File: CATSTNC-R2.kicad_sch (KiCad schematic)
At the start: 64 parts, among them J1 BNC, J1 USB_C_Receptacle_USB2.0, J4 GPIO-1, J5 DC IN, J5 GPIO-2, SW1 BOOT, SW1 RESET, U1 RP2040, U1 TPS62933, U4 NCP1117-3.3_SOT223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

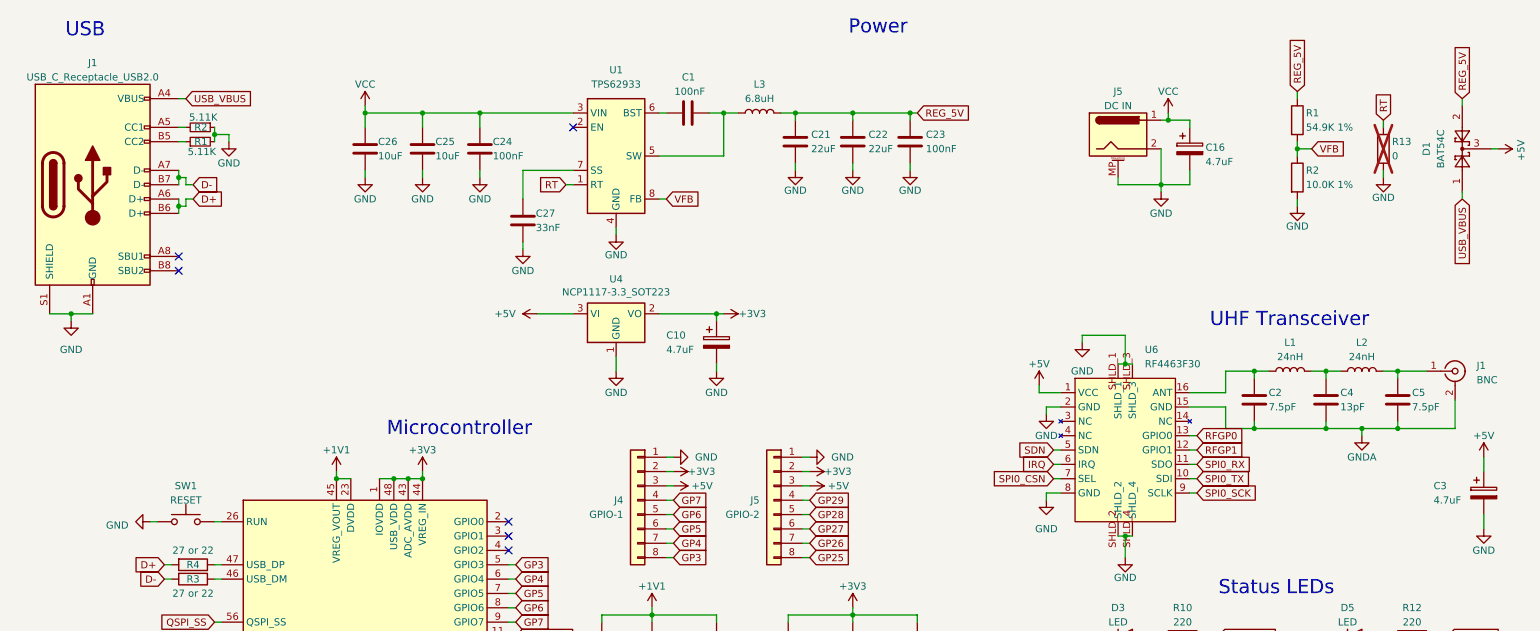
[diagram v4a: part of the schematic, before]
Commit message: Remove BAT54C
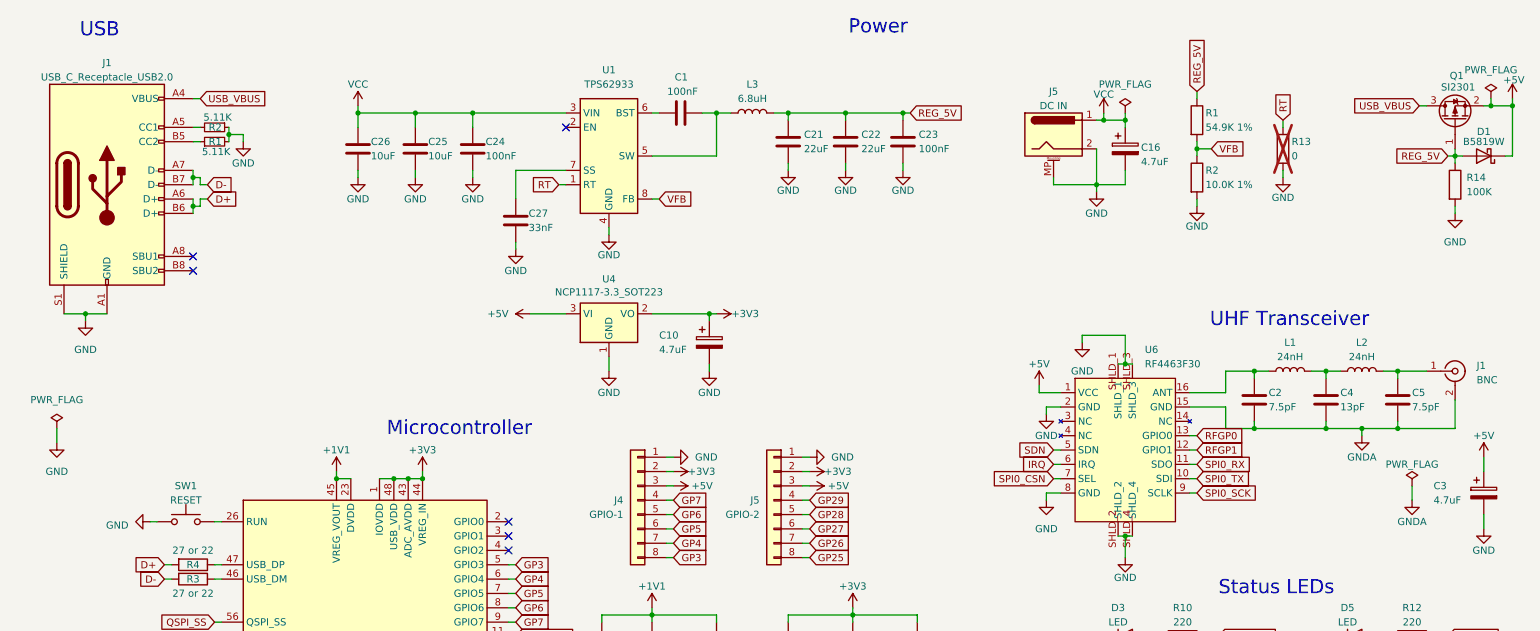
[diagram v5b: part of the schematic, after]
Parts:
- removed D1: BAT54C, Package_TO_SOT_SMD:SOT-23, symbol Diode:BAT54C
- added D1: B5819W, Diode_SMD:D_SOD-123, symbol Device:D_Schottky
- added Q1: SI2301, Package_TO_SOT_SMD:SOT-23, symbol Transistor_FET:FDN340P
- added R14: 100K, Resistor_SMD:R_0603_1608Metric, symbol Device:R
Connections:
- net +5V: now also D1.1 (K), Q1.2 (S)
- net GND: now also R14.2
- net REG_5V: now also D1.2 (A), Q1.1 (G), R14.1
- net USB_VBUS: now also Q1.3 (D)
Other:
- moved on the sheet: C1, C10, C16, C21, C22, C23, C24, C25, C26, C27, J1, J5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

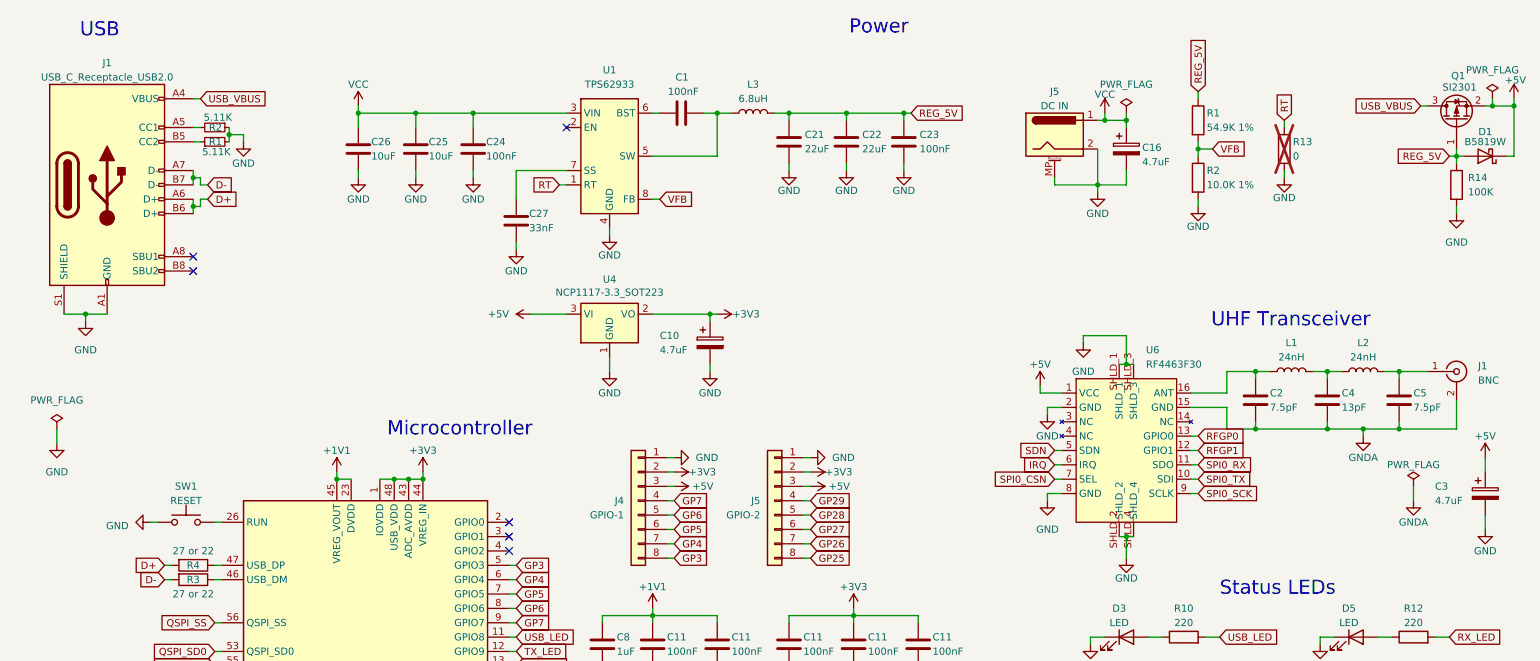
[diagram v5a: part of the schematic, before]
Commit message: Add power mux, USB TVS
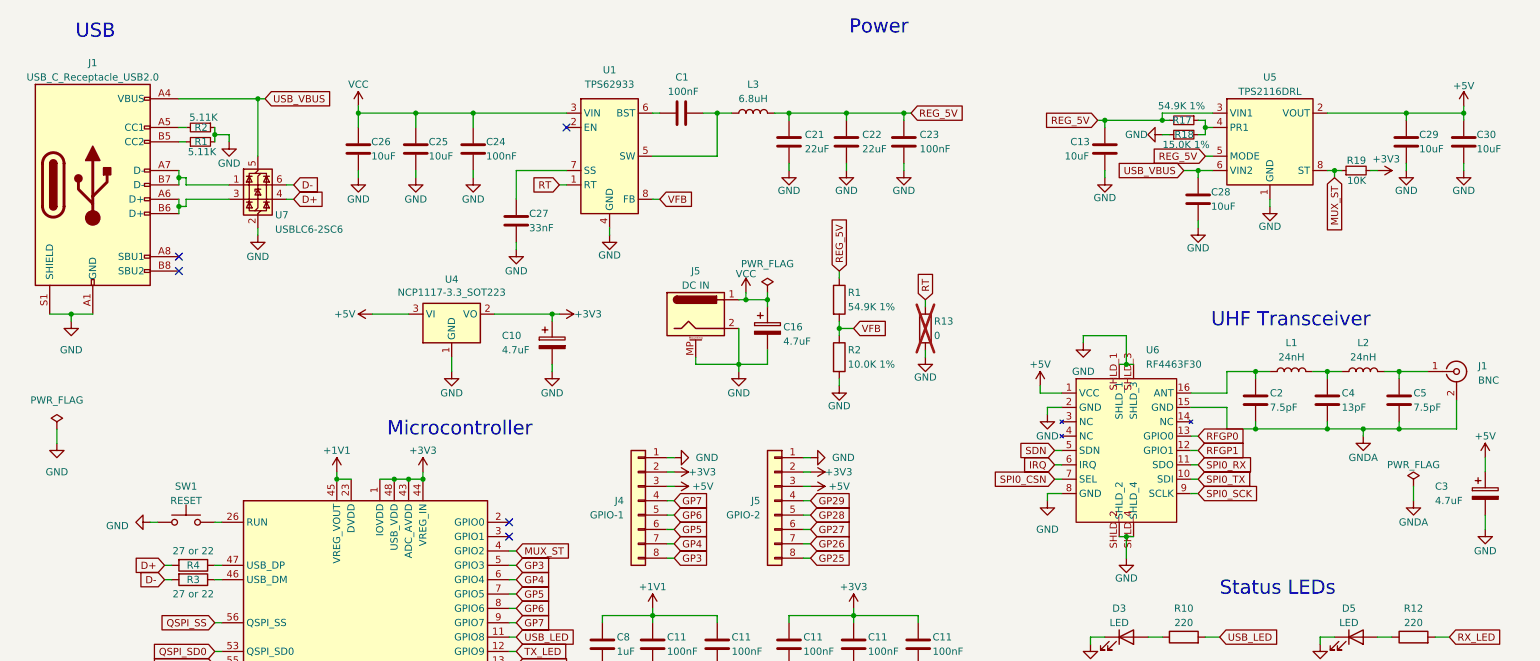
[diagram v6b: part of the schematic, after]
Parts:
- removed D1: B5819W, Diode_SMD:D_SOD-123, symbol Device:D_Schottky
- removed Q1: SI2301, Package_TO_SOT_SMD:SOT-23, symbol Transistor_FET:FDN340P
- removed R14: 100K, Resistor_SMD:R_0603_1608Metric, symbol Device:R
- added C13, C28, C29, C30: 10uF, Capacitor_SMD:C_0402_1005Metric, symbol Device:C
- added R17: 54.9K 1%, Resistor_SMD:R_0402_1005Metric, symbol Device:R_Small
- added R18: 15.0K 1%, Resistor_SMD:R_0402_1005Metric, symbol Device:R_Small
- added R19: 10K, Resistor_SMD:R_0402_1005Metric, symbol Device:R_Small
- added U5: TPS2116DRL, Package_TO_SOT_SMD:SOT-583-8, symbol Power_Management:TPS2116DRL
- added U7: USBLC6-2SC6, Package_TO_SOT_SMD:SOT-23-6, symbol Power_Protection:USBLC6-2SC6
- C21, C22, C23: footprint Capacitor_SMD:C_0603_1608Metric -> Capacitor_SMD:C_0402_1005Metric
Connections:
- net +3V3: now also R19.2
- net +5V: now also C29.1, C30.1, U5.2 (VOUT), U5.7 (VOUT)
- net D+: now also U7.4 (I/O2); no longer J1.A6 (D+), J1.B6 (D+)
- net D-: now also U7.6 (I/O1); no longer J1.A7 (D-), J1.B7 (D-)
- net GND: now also C13.2, C28.2, C29.2, C30.2, R18.1, U5.1 (GND), U7.2 (GND)
- net REG_5V: now also C13.1, R17.2, U5.3 (VIN1), U5.5 (MODE)
- net USB_VBUS: now also C28.1, U5.6 (VIN2), U7.5 (VBUS)
- net MUX_ST: now reaches U1.4 (GPIO2)
- net MUX_ST: now also R19.1, U5.8 (ST)
- new net: R17.1, R18.2, U5.4 (PR1)
- new net: J1.A7 (D-), J1.B7 (D-), U7.1 (I/O1)
- new net: J1.A6 (D+), J1.B6 (D+), U7.3 (I/O2)
- no-connect marks 14 -> 13
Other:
- moved on the sheet: C10, C16, J1, J5, R1, R13, R2, U4

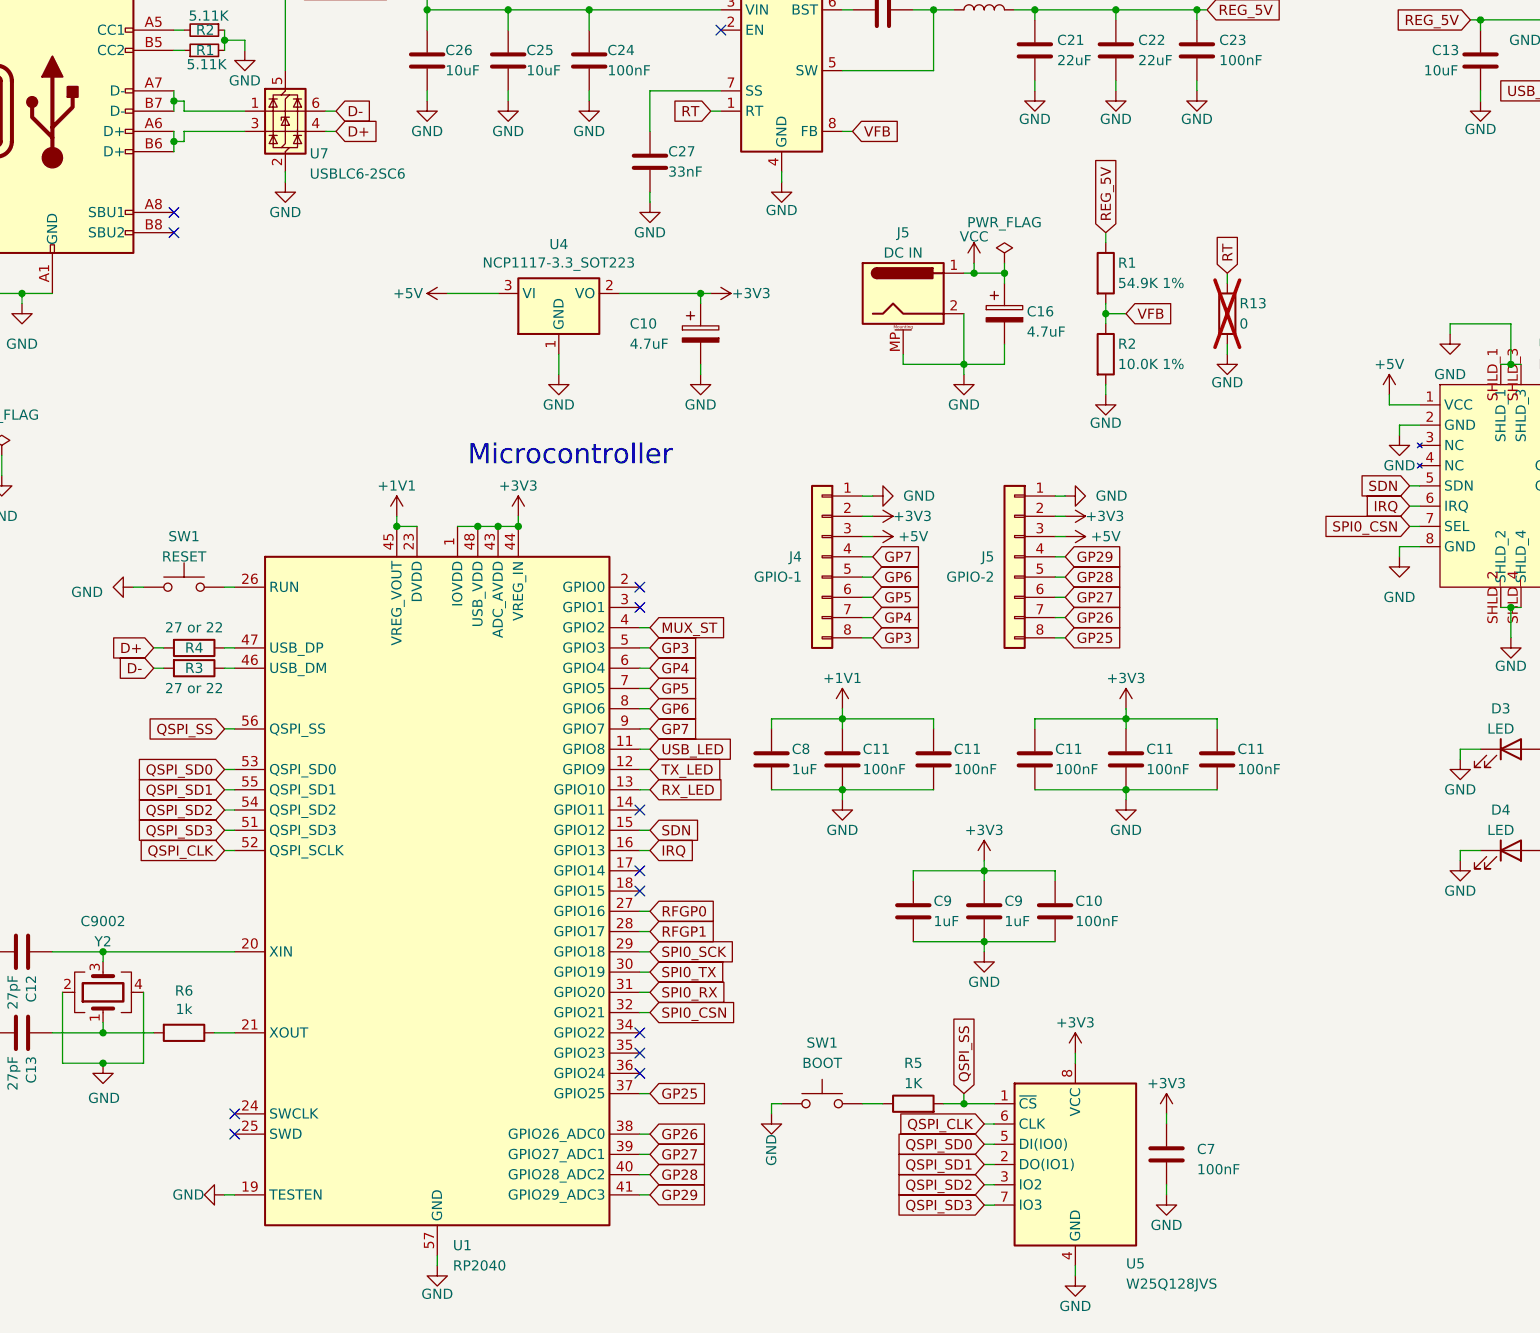
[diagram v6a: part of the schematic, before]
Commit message: Add SWD header, VCC voltmeter, replace GP29 with VIN
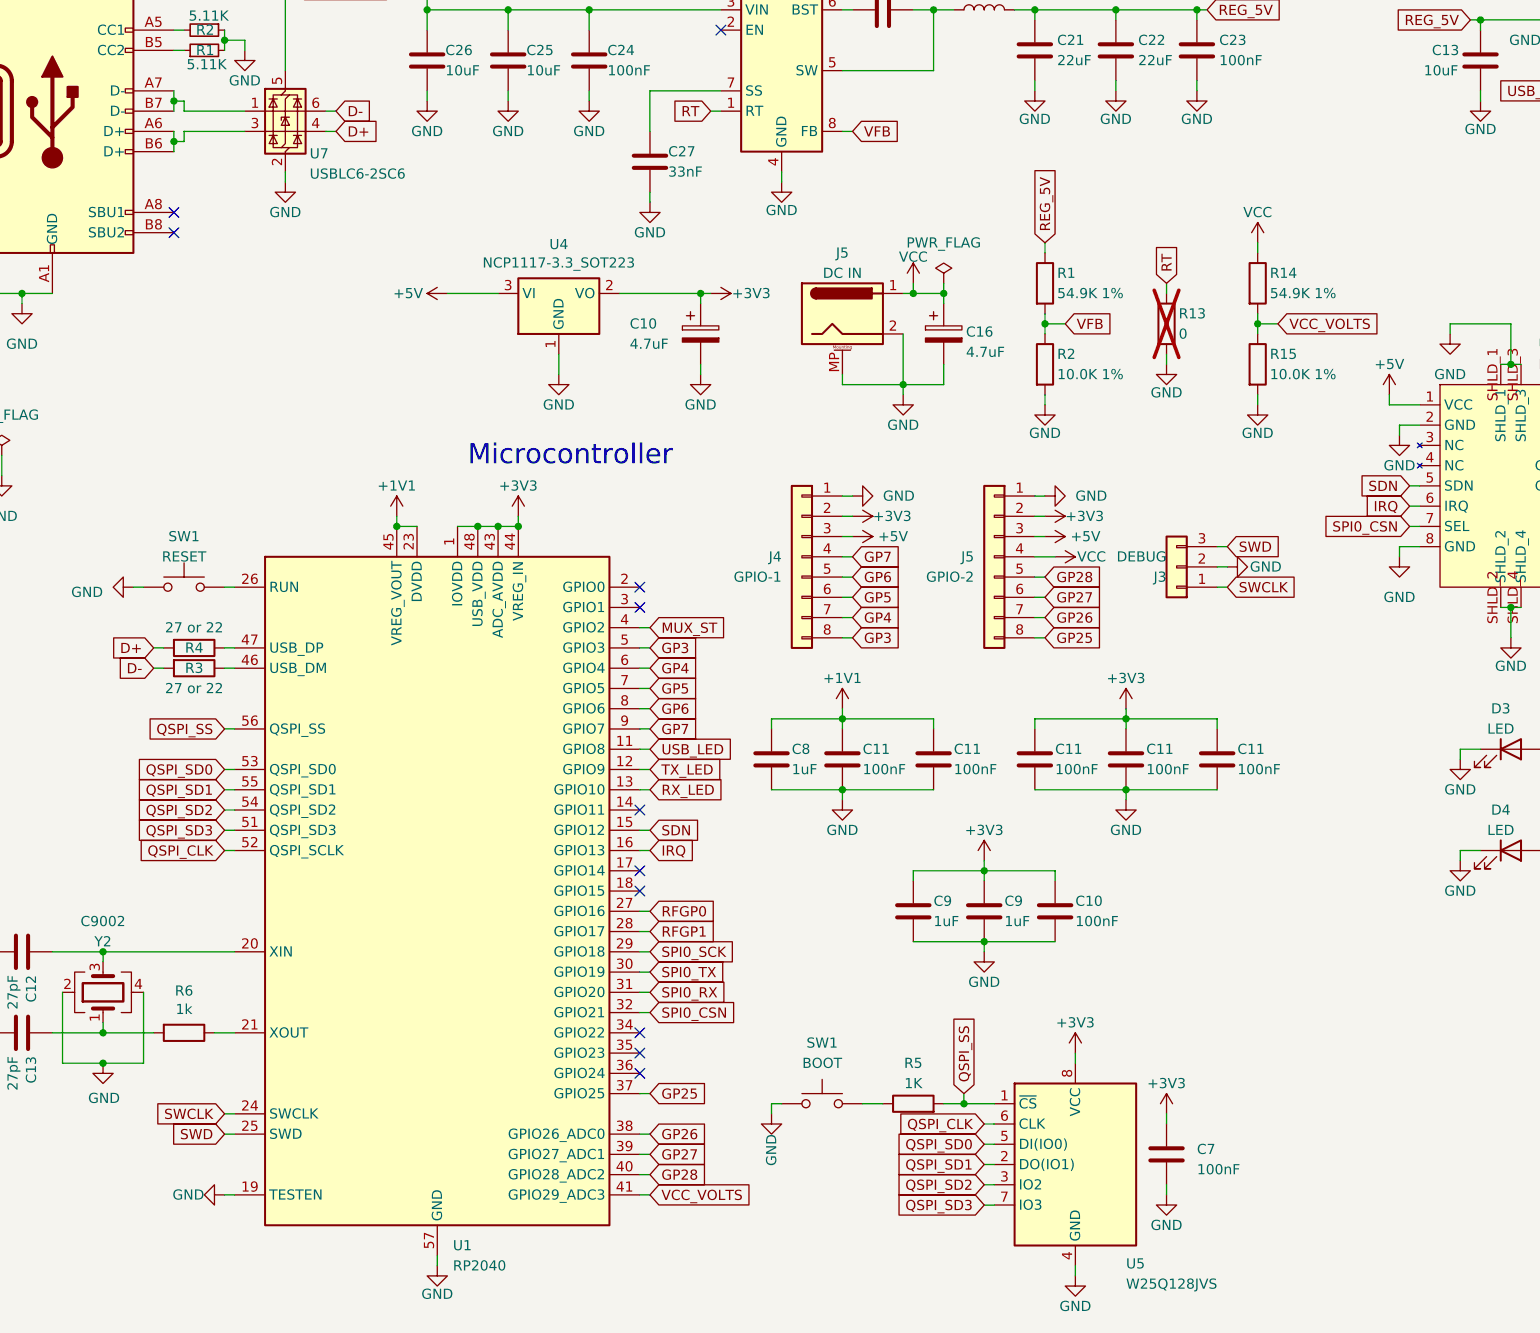
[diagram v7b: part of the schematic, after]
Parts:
- added J3: DEBUG, Connector_PinHeader_2.54mm:PinHeader_1x03_P2.54mm_Vertical, symbol Connector_Generic:Conn_01x03
- added R14: 54.9K 1%, Resistor_SMD:R_0402_1005Metric, symbol Device:R
- added R15: 10.0K 1%, Resistor_SMD:R_0402_1005Metric, symbol Device:R
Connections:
- net GND: now also J3.2 (Pin_2), R15.2
- net VCC: now also J5.4 (Pin_4), R14.1
- net SWCLK: now reaches U1.24 (SWCLK)
- net SWCLK: now also J3.1 (Pin_1)
- net SWD: now reaches U1.25 (SWD)
- net SWD: now also J3.3 (Pin_3)
- net GP29 renamed VCC_VOLTS
- net VCC_VOLTS: now also R14.2, R15.1; no longer J5.4 (Pin_4)
- no-connect marks 13 -> 11
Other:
- moved on the sheet: C16, J4, J5, R1, R13, R2

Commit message: Did some stuff idk
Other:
- note added: "3.3V Regulator"
- note added: "5V Buck Converter"
- note added: "GPIO"
- note added: "Power MUX"
- note added: "SPI Flash"
- note removed: "Power"
- moved on the sheet: C1, C10, C11, C12, C13, C16, C2, C21, C22, C23, C24, C25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
